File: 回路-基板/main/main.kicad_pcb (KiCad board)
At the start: 2 copper layers, 70 x 70 mm, 31 parts, among them J2 Conn_01x06_Pin, Q1 PNP, Q2 NPN, Q3 PNP, Q4 NPN, SW1 SW_Push, SW2 SW_Push, SW3 SW_Push, SW4 SW_Push, SW5 SW_Push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

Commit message: 回路やり直したよ
山本さんからのアドバイス部分を修正
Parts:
- C1, C2, C3: moved to F.Cu
- moved C3 75.6 mm to (85.5, 101.0), turned to 90 degrees
- moved C2 72.2 mm to (83.0, 101.0), turned to 90 degrees
- moved C1 68.9 mm to (80.5, 101.0), turned to 90 degrees
- moved C4 31.1 mm to (109.2, 139.0)
- moved R3 31.1 mm to (103.3, 146.0)
- moved R4 31.1 mm to (115.2, 139.0)
- moved R5 31.1 mm to (115.2, 141.9)
- moved R7 31.1 mm to (92.9, 141.0)
- moved R8 31.1 mm to (92.9, 143.9)
- moved C5 31.1 mm to (109.2, 143.7)
- moved R6 31.1 mm to (115.2, 144.9)
- moved R9 31.1 mm to (92.9, 146.9)
- moved R1 31.1 mm to (97.1, 145.0)
- moved R2 31.1 mm to (97.1, 147.9)
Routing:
- net VCC: track 37.5 -> 44.9 mm, vias 1 -> 2

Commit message: 回路関連
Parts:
- added C10: 0.1uF, Capacitor_SMD:C_0805_2012Metric, B.Cu at (59.7, 111.4)
- added C6: 0.1uF, Capacitor_SMD:C_0805_2012Metric, B.Cu at (66.2, 111.4)
- added C7: 0.1uF, Capacitor_SMD:C_0805_2012Metric, B.Cu at (72.7, 111.4)
- added C8: 0.1uF, Capacitor_SMD:C_0805_2012Metric, B.Cu at (66.2, 115.9)
- added C9: 0.1uF, Capacitor_SMD:C_0805_2012Metric, B.Cu at (66.2, 107.4)
- added FB: 120Ω, Inductor_SMD:L_0603_1608Metric, B.Cu at (92.2, 114.7)
- added N-R: Jumper_2_Small_Bridged, Jumper:SolderJumper-2_P1.3mm_Bridged_Pad1.0x1.5mm, B.Cu at (97.4, 80.4)
- added N-R: Jumper_2_Small_Bridged, Jumper:SolderJumper-2_P1.3mm_Bridged_Pad1.0x1.5mm, B.Cu at (97.4, 82.9)
- added R: Jumper_2_Small_Open, Jumper:SolderJumper-2_P1.3mm_Open_Pad1.0x1.5mm, B.Cu at (113.2, 82.4)
- added R: Jumper_2_Small_Open, Jumper:SolderJumper-2_P1.3mm_Open_Pad1.0x1.5mm, B.Cu at (113.2, 84.9)
- added R10: 10K, Resistor_SMD:R_0805_2012Metric, B.Cu at (67.5, 77.4)
- added R11: 10K, Resistor_SMD:R_0805_2012Metric, B.Cu at (70.0, 77.4)
- added R12: 100, Resistor_SMD:R_0805_2012Metric, B.Cu at (109.4, 82.4)
- added R13: 100, Resistor_SMD:R_0805_2012Metric, B.Cu at (109.4, 84.9)
- C4, C5: moved to F.Cu
- moved R9 84.1 mm to (91.7, 62.9), turned to -135 degrees
- moved R5 83.5 mm to (89.0, 62.6), turned to 45 degrees
- moved R7 76.6 mm to (93.2, 64.4), turned to -135 degrees
- moved R4 63.8 mm to (57.7, 111.4), turned to 90 degrees
- moved C5 60.3 mm to (73.6, 95.0), turned to 90 degrees
- moved C4 58.2 mm to (71.2, 94.9), turned to 90 degrees
- moved R6 52.6 mm to (74.7, 111.4), turned to 90 degrees
- moved R8 46.9 mm to (66.2, 105.4), turned to 0 degrees
- moved R3 46.5 mm to (66.2, 117.9), turned to 0 degrees
- moved R2 40.4 mm to (66.2, 121.9)
- moved R1 39.8 mm to (66.2, 119.9), turned to 0 degrees
- moved BT1 17.9 mm to (66.2, 94.9)
- moved BT2 17.9 mm to (100.2, 94.9)
- moved C1 17.9 mm to (63.7, 94.9)
- moved C2 17.9 mm to (66.2, 94.9)
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- renumbered Q2 to NPN, Q4 to NPN, Q3 to PNP, Q1 to PNP
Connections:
- J2 pad 4: USB-TX=main -> Net-(J2-Pin_4)
- J2 pad 5: USB-RX=main -> Net-(J2-Pin_5)
- U4 pad 1: +3.3V -> GPS-TX=main
- U4 pad 2: GPS-TX=main -> GND
- U4 pad 4: GND -> unconnected-(U4-BATT-Pad4)
- U4 pad 5: (no net) -> Net-(U4-VCC)
- U4 pad 6: (no net) -> unconnected-(U4-NC-Pad6)
- U4 pad 7: (no net) -> unconnected-(U4-NC-Pad7)
- U4 pad 8: (no net) -> unconnected-(U4-NC-Pad8)
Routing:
- net BTN-CENTER: track 0.00 -> 97.6 mm, vias 0 -> 2
- net BTN-UP: track 0.00 -> 91.3 mm, vias 0 -> 2
- net BTN-LEFT: track 0.00 -> 81.8 mm, vias 0 -> 2
- net BTN-DOWN: track 0.00 -> 72.4 mm, vias 0 -> 2
- net +3.3V: track 59.0 -> 131.1 mm, vias 0 -> 3
- net BTN-RIGHT: track 0.00 -> 68.7 mm, vias 0 -> 2
- net RX=main: track 3.12 -> 47.1 mm, vias 2 -> 3
- net Net-(C10-Pad1): track 0.00 -> 42.7 mm
- net TX=main: track 7.71 -> 38.0 mm, vias 1 -> 0
- net RTS=main: track 0.00 -> 22.7 mm, vias 0 -> 2
- net Net-(J2-Pin_5): track 0.00 -> 21.8 mm
- net Net-(J2-Pin_4): track 0.00 -> 19.4 mm
- net USB-TX=main: track 6.32 -> 23.7 mm, vias 0 -> 1
- net CTS=main: track 0.00 -> 15.4 mm, vias 0 -> 1
- net UART-GPS=ON: track 57.5 -> 68.1 mm
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
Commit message: 事後プレゼンスライド追加
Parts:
- removed BT1, BT2: 3V, @2024-cansat:BHSD-2032-SM
- removed C1, C10, C6, C7, C8, C9: 0.1uF, Capacitor_SMD:C_0805_2012Metric
- removed C2, C4, C5: 10uF, Capacitor_SMD:C_0805_2012Metric
- removed C3: 22uF, Capacitor_SMD:C_0805_2012Metric
- removed FB: 120Ω, Inductor_SMD:L_0603_1608Metric
- removed J2: Conn_01x06_Pin, Connector_PinSocket_2.54mm:PinSocket_1x06_P2.54mm_Horizontal
- removed N-R (x2): Jumper_2_Small_Bridged, Jumper:SolderJumper-2_P1.3mm_Bridged_Pad1.0x1.5mm
- removed NPN (x2): NPN, Package_TO_SOT_SMD:SC-59
- removed PNP (x2): PNP, Package_TO_SOT_SMD:SOT-323_SC-70
- removed R (x2): Jumper_2_Small_Open, Jumper:SolderJumper-2_P1.3mm_Open_Pad1.0x1.5mm
- removed R1, R3, R4, R6, R7, R8, R9: 100k, Resistor_SMD:R_0805_2012Metric
- removed R10, R11: 10K, Resistor_SMD:R_0805_2012Metric
- removed R12, R13: 100, Resistor_SMD:R_0805_2012Metric
- removed R2, R5: 10k, Resistor_SMD:R_0805_2012Metric
- removed SW1, SW2, SW3, SW4, SW5: SW_Push, @2024-cansat:TVBP06-B043C
- removed SW6: SW_SPDT, @2024-cansat:SS12D01G4
- removed U1: TWE-L-WX, RF_Module:MonoWireless_TWE-L-WX
- removed U2: ~, Connector_PinSocket_2.54mm:PinSocket_1x04_P2.54mm_Vertical
- removed U3: LM1117MP-3.3, Package_TO_SOT_SMD:SOT-223-3_TabPin2
- removed U4: ~, @2024-cansat:GPS-54D-014
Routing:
- net +3.3V: track 131.1 -> 0.00 mm, vias 3 -> 0
- net BTN-CENTER: track 97.6 -> 0.00 mm, vias 2 -> 0
- net BTN-UP: track 91.3 -> 0.00 mm, vias 2 -> 0
- net BTN-LEFT: track 81.8 -> 0.00 mm, vias 2 -> 0
- net BTN-DOWN: track 72.4 -> 0.00 mm, vias 2 -> 0
- net BTN-RIGHT: track 68.7 -> 0.00 mm, vias 2 -> 0
- net UART-GPS=ON: track 68.1 -> 0.00 mm, vias 1 -> 0
- net VCC: track 47.4 -> 0.00 mm, vias 2 -> 0
- net RX=main: track 47.1 -> 0.00 mm, vias 3 -> 0
- net Net-(C10-Pad1): track 42.7 -> 0.00 mm
- net SCL: track 40.6 -> 0.00 mm
- net TX=main: track 38.0 -> 0.00 mm
- net SDA: track 33.1 -> 0.00 mm
- net USB-TX=main: track 23.7 -> 0.00 mm, vias 1 -> 0
- net UART-USB=ON: track 22.9 -> 0.00 mm
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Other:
- board size 70 x 70 mm -> 60 x 60 mm
- board text added: "・TWE-LITEのアンテナは中心になってはいけない （重ねたときに互い違いにするため） アンテナ筒の外径=8mm →最低4mmずらすことが必要 ・原点中心で対角に穴を作る（最低直径3mm）"

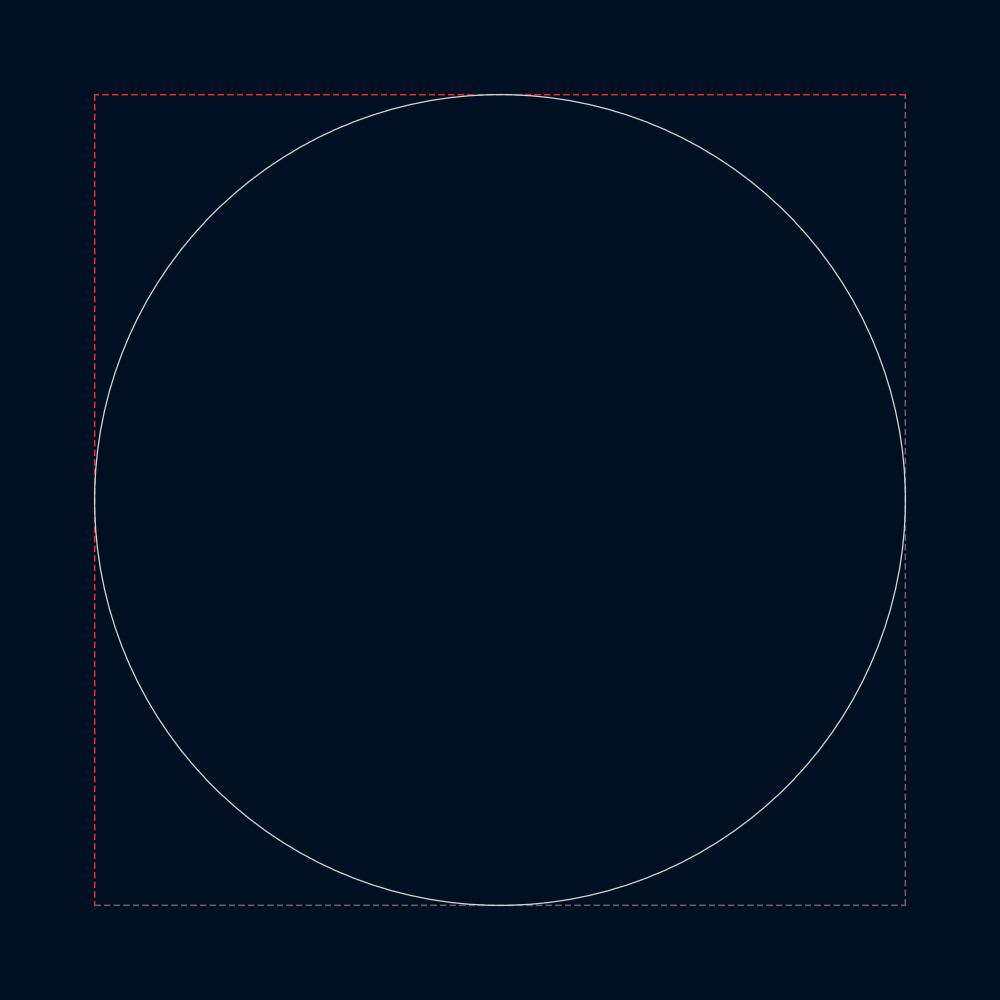
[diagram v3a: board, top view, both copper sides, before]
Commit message: 回路図を修正、PCBを作成し始めた（直径60）
電池の配置場所がわからん...
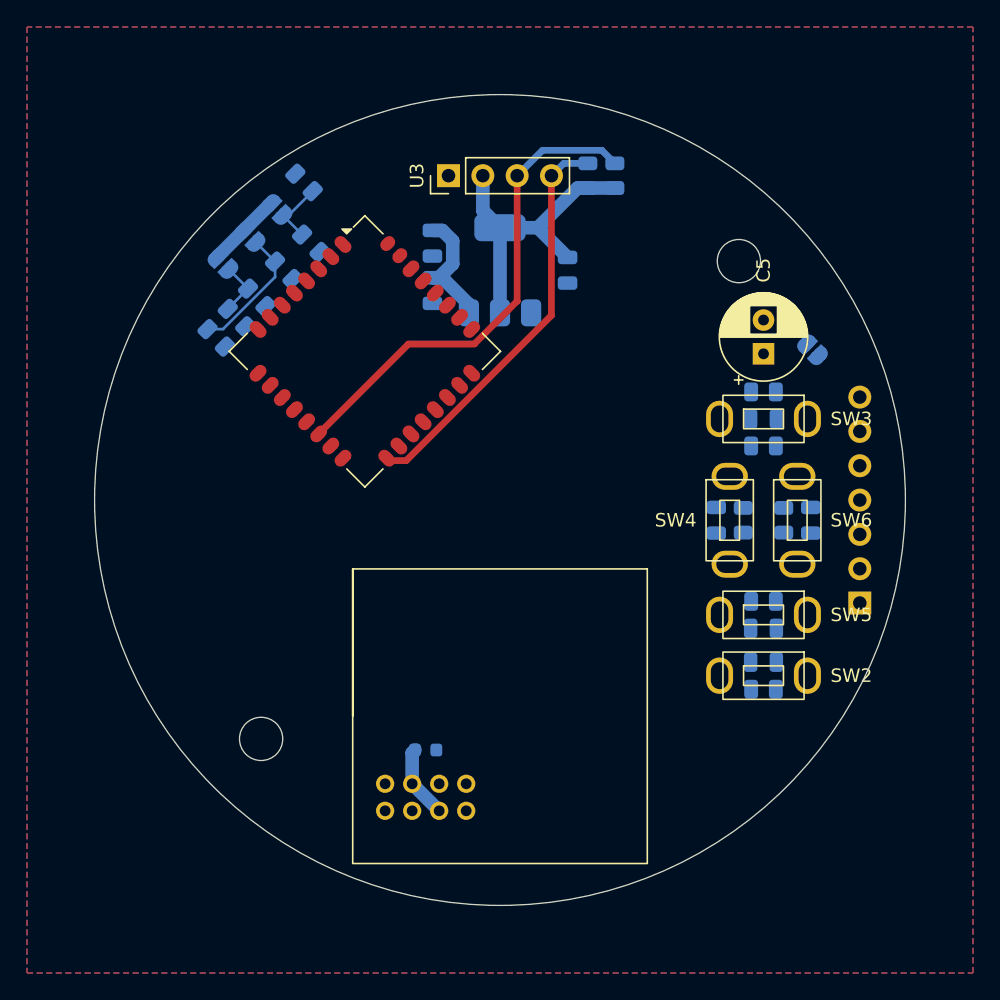
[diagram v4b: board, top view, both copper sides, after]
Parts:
- added C1: 0.1uF, Capacitor_SMD:C_0805_2012Metric, B.Cu at (-5.00, -19.0)
- added C10: 0.1uF, Capacitor_SMD:C_0805_2012Metric, B.Cu at (23.0, 1.50)
- added C3: 10uF, Capacitor_SMD:C_0805_2012Metric, B.Cu at (-5.00, -15.5)
- added C4: 10uF, Capacitor_SMD:C_0805_2012Metric, B.Cu at (5.00, -17.0)
- added C5: 100uF, Capacitor_THT:CP_Radial_D6.3mm_P2.50mm, F.Cu at (19.5, -10.8)
- added C6: 0.1uF, Capacitor_SMD:C_0805_2012Metric, B.Cu at (19.5, 12.0)
- added C7: 0.1uF, Capacitor_SMD:C_0805_2012Metric, B.Cu at (19.5, -6.00)
- added C8: 0.1uF, Capacitor_SMD:C_0805_2012Metric, B.Cu at (16.0, 1.50)
- added C9: 0.1uF, Capacitor_SMD:C_0805_2012Metric, B.Cu at (19.5, 9.50)
- added FB1: FerriteBead_Small, Inductor_SMD:L_0603_1608Metric, B.Cu at (-5.50, 18.5)
- added J1: Conn_01x07_Pin, Connector_PinHeader_2.54mm:PinHeader_1x07_P2.54mm_Horizontal, B.Cu at (26.6, 7.62)
- added JP1: Jumper_2_Small_Open, Jumper:SolderJumper-2_P1.3mm_Open_RoundedPad1.0x1.5mm, B.Cu at (23.1, -11.1)
- added JP2: Jumper_2_Small_Open, Jumper:SolderJumper-2_P1.3mm_Open_RoundedPad1.0x1.5mm, B.Cu at (-16.5, -21.5)
- added JP3: Jumper_2_Small_Open, Jumper:SolderJumper-2_P1.3mm_Open_RoundedPad1.0x1.5mm, B.Cu at (-18.5, -19.5)
- added JP4: Jumper_2_Small_Open, Jumper:SolderJumper-2_P1.3mm_Open_RoundedPad1.0x1.5mm, B.Cu at (-20.5, -17.5)
- added R10: 10K, Resistor_SMD:R_0805_2012Metric, B.Cu at (8.50, -24.0)
- added R11: 10K, Resistor_SMD:R_0805_2012Metric, B.Cu at (6.50, -24.0)
- added R12: 100k, Resistor_SMD:R_0805_2012Metric, B.Cu at (19.5, 14.0)
- added R13: 100k, Resistor_SMD:R_0805_2012Metric, B.Cu at (19.5, -4.00)
- added R14: 100k, Resistor_SMD:R_0805_2012Metric, B.Cu at (18.0, 1.50)
- added R15: 100k, Resistor_SMD:R_0805_2012Metric, B.Cu at (19.5, 7.50)
- added R16: 100k, Resistor_SMD:R_0805_2012Metric, B.Cu at (21.0, 1.50)
- added R17: 10k, Resistor_SMD:R_0805_2012Metric, B.Cu at (19.5, -8.00)
- added R4: 1K, Resistor_SMD:R_0805_2012Metric, B.Cu at (-14.0, -19.0)
- added R5: 10K, Resistor_SMD:R_0805_2012Metric, B.Cu at (-14.5, -23.5)
- added R6: 1K, Resistor_SMD:R_0805_2012Metric, B.Cu at (-16.0, -17.0)
- added R7: 10K, Resistor_SMD:R_0805_2012Metric, B.Cu at (-21.0, -12.0)
- added R8: 1K, Resistor_SMD:R_0805_2012Metric, B.Cu at (-18.0, -15.0)
- added R9: 10K, Resistor_SMD:R_0805_2012Metric, B.Cu at (-19.5, -13.5)
- added REF**: MountingHole_3.2mm_M3, MountingHole:MountingHole_3.2mm_M3, F.Cu at (-17.7, 17.7)
- added REF**: MountingHole_3.2mm_M3, MountingHole:MountingHole_3.2mm_M3, F.Cu at (17.7, -17.7)
- added SW2: SW_Push, @2024-cansat:TVBP06-B043C, F.Cu at (19.5, 13.0)
- added SW3: SW_Push, @2024-cansat:TVBP06-B043C, F.Cu at (19.5, -6.00)
- added SW4: SW_Push, @2024-cansat:TVBP06-B043C, F.Cu at (17.0, 1.50)
- added SW5: SW_Push, @2024-cansat:TVBP06-B043C, F.Cu at (19.5, 8.50)
- added SW6: SW_Push, @2024-cansat:TVBP06-B043C, F.Cu at (22.0, 1.50)
- added U1: TWE-L-WX, RF_Module:MonoWireless_TWE-L-WX, F.Cu at (-10.0, -11.0)
- added U2: LM1117MP-3.3, Package_TO_SOT_SMD:SOT-223-3_TabPin2, B.Cu at (0.00, -17.0)
- added U3: ~, @2024-cansat:Display, F.Cu at (0.00, -24.0)
- added U4: ~, @2024-cansat:GPS-54D-014, F.Cu at (0.00, 16.0)
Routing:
- net 14: track 0.00 -> 36.4 mm
- net 17: track 0.00 -> 30.1 mm
- net +3.3V: track 0.00 -> 29.2 mm
- net Net-(JP3-A): track 0.00 -> 9.72 mm
- net VCC: track 0.00 -> 9.59 mm
- net Net-(U4-BATT): track 0.00 -> 5.42 mm
- net Net-(JP2-A): track 0.00 -> 4.91 mm
- net Net-(JP4-A): track 0.00 -> 4.09 mm
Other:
- board text removed: "・TWE-LITEのアンテナは中心になってはいけない （重ねたときに互い違いにするため） アンテナ筒の外径=8mm →最低4mmずらすことが必要 ・原点中心で対角に穴を作る（最低直径3mm）"

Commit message: PCBデザインを更新
単4電池3本分のサイズをとってみた、きつい
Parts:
- C1, C3, C4, JP2, JP3, JP4, R4, R5, R6, R7, R8, R9, U2: moved to F.Cu
- moved R4 35.0 mm to (-43.2, 0.34), turned to 0 degrees
- moved R6 33.9 mm to (-43.2, 3.17), turned to 0 degrees
- moved R8 32.8 mm to (-43.2, 6.00), turned to 0 degrees
- moved R5 32.8 mm to (-39.6, -2.49), turned to 180 degrees
- moved R9 32.1 mm to (-43.2, 8.12), turned to 0 degrees
- moved JP2 31.8 mm to (-39.6, 0.34), turned to 0 degrees
- moved R7 31.4 mm to (-43.2, 10.2), turned to 0 degrees
- moved JP3 31.0 mm to (-39.6, 3.17), turned to 0 degrees
- moved JP4 30.3 mm to (-39.6, 6.00), turned to 0 degrees
- moved C3 8.06 mm to (-6.00, -23.5), turned to 180 degrees
- moved C4 6.58 mm to (6.00, -23.5), turned to 0 degrees
- moved C1 6.36 mm to (-9.50, -23.5), turned to 0 degrees
- moved U2 3.50 mm to (0.00, -20.5), turned to -90 degrees
- moved U3 3.50 mm to (0.00, -27.5)
- moved FB1 2.50 mm to (-5.50, 21.0)
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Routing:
- net +3.3V: track 29.2 -> 0.00 mm
- net 14: track 36.4 -> 9.22 mm
- net 17: track 30.1 -> 3.35 mm
- net Net-(JP3-A): track 9.72 -> 0.00 mm
- net VCC: track 9.59 -> 0.00 mm
- net Net-(JP2-A): track 4.91 -> 0.00 mm
- net Net-(JP4-A): track 4.09 -> 0.00 mm

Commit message: 回路図/PCB両方一応完成した
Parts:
- removed C10: 0.1uF, Capacitor_SMD:C_0805_2012Metric
- removed JP1, JP2, JP3, JP4: Jumper_2_Small_Open, Jumper:SolderJumper-2_P1.3mm_Open_RoundedPad1.0x1.5mm
- removed R15, R16: 100k, Resistor_SMD:R_0805_2012Metric
- removed R17: 10k, Resistor_SMD:R_0805_2012Metric
- removed SW6: SW_Push, @2024-cansat:TVBP06-B043C
- added BT1: 1.5V, @2024-cansat:AAA-holder, B.Cu at (12.0, -22.4)
- added BT2: 1.5V, @2024-cansat:AAA-holder, B.Cu at (0.00, 22.4)
- added BT3: 1.5V, @2024-cansat:AAA-holder, B.Cu at (-12.0, -22.4)
- added C2: 10uF, Capacitor_SMD:C_0805_2012Metric, F.Cu at (-16.0, -13.0)
- added J2: Conn_01x08_Pin, @2024-cansat:Pin-Extender, F.Cu at (16.4, -20.1)
- added J3: Conn_01x08_Pin, @2024-cansat:Pin-Extender, F.Cu at (2.44, -14.9)
- added J4: Conn_01x08_Pin, @2024-cansat:Pin-Extender, F.Cu at (7.55, -0.94)
- added J5: Conn_01x08_Pin, @2024-cansat:Pin-Extender, F.Cu at (21.6, -6.05)
- added M1: Jumper_2_Small_Open, Jumper:SolderJumper-2_P1.3mm_Open_RoundedPad1.0x1.5mm, B.Cu at (-2.50, -16.0)
- added M2: Jumper_2_Small_Open, Jumper:SolderJumper-2_P1.3mm_Open_RoundedPad1.0x1.5mm, B.Cu at (-2.50, -11.5)
- added M3: Jumper_2_Small_Open, Jumper:SolderJumper-2_P1.3mm_Open_RoundedPad1.0x1.5mm, B.Cu at (-2.50, -7.00)
- added R1: 1K, Resistor_SMD:R_0805_2012Metric, F.Cu at (-2.50, -17.0)
- added R2: 10K, Resistor_SMD:R_0805_2012Metric, F.Cu at (-2.50, -15.0)
- added R3: 1K, Resistor_SMD:R_0805_2012Metric, F.Cu at (-2.50, -12.5)
- added SW1: SW_Push, @2024-cansat:TVBP06-B043C, F.Cu at (12.0, 11.0)
- added VBUS/+3.3V: Jumper_2_Small_Open, Jumper:SolderJumper-2_P1.3mm_Open_RoundedPad1.0x1.5mm, B.Cu at (22.9, 0.50)
- C4: value 10uF -> 100uF; footprint Capacitor_SMD:C_0805_2012Metric -> Capacitor_THT:CP_Radial_D6.3mm_P2.50mm
- C5: value 100uF -> 0.1uF; footprint Capacitor_THT:CP_Radial_D6.3mm_P2.50mm -> Capacitor_SMD:C_0805_2012Metric
- C6, C7, C8, C9, FB1, R12, R13: moved to F.Cu
- J1: footprint Connector_PinHeader_2.54mm:PinHeader_1x07_P2.54mm_Horizontal -> Connector_PinSocket_2.54mm:PinSocket_1x07_P2.54mm_Vertical; moved to F.Cu
- R10, R11: value 10K -> 100k; moved to F.Cu
- R14: value 100k -> 10k; moved to F.Cu
- R4, R6, R8: value 1K -> 10K
- R5: value 10K -> 1K
- R9: value 10K -> 100k
- moved R8 59.3 mm to (7.00, -25.5), turned to 90 degrees
- moved R9 57.2 mm to (14.0, 8.00), turned to 180 degrees
- moved R7 50.9 mm to (-7.00, -25.5), turned to 90 degrees
- moved R4 42.1 mm to (-2.50, -10.5)
- moved R6 41.7 mm to (-2.50, -6.00)
- moved REF** 37.6 mm to (19.9, 18.2), turned to 2.5 degrees
- moved REF** 37.6 mm to (-19.9, -18.2), turned to 2.5 degrees
- moved R5 37.6 mm to (-2.50, -8.00)
- moved R11 33.9 mm to (1.00, 8.50), turned to -90 degrees
- moved C4 29.8 mm to (-20.5, -9.85), turned to 180 degrees
- moved FB1 28.2 mm to (-19.5, -3.50)
- moved R10 26.6 mm to (14.0, 1.00), turned to 180 degrees
- moved C7 26.2 mm to (1.00, 12.5), turned to 90 degrees
- moved SW3 23.0 mm to (4.00, 11.0), turned to -90 degrees
- moved U1 22.0 mm to (12.0, -10.5), turned to -90 degrees
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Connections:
- C3 pad 1: VCC -> +3.3V
- C5 pad 1: +3.3V -> Net-(C5-Pad1)
- C5 pad 2: GND -> 23
- C6 pad 1: Net-(C10-Pad1) -> Net-(C5-Pad1)
- C6 pad 2: BTN-CENTER -> 25
- C7 pad 1: Net-(C10-Pad1) -> Net-(C5-Pad1)
- C7 pad 2: BTN-UP -> 22
- C8 pad 1: Net-(C10-Pad1) -> Net-(C5-Pad1)
- C8 pad 2: BTN-LEFT -> 19
- C9 pad 1: Net-(C10-Pad1) -> Net-(C5-Pad1)
- C9 pad 2: BTN-DOWN -> 24
- J1 pad 6: +3.3V -> Net-(J1-Pin_6)
- J1 pad 7: Net-(J1-Pin_7) -> unconnected-(J1-Pin_7-Pad7)
- R10 pad 1: +3.3V -> GND
- R10 pad 2: 14 -> 25
- R11 pad 1: +3.3V -> GND
- R11 pad 2: 17 -> 22
- R12 pad 2: BTN-CENTER -> 19
- R13 pad 2: BTN-UP -> 24
- R14 pad 1: GND -> +3.3V
- R14 pad 2: BTN-LEFT -> Net-(C5-Pad1)
- R4 pad 1: 12 -> GND
- R4 pad 2: Net-(JP2-A) -> Net-(JP3-A)
- R5 pad 1: GND -> 27
- R5 pad 2: Net-(JP2-A) -> Net-(JP4-A)
- R6 pad 1: 26 -> GND
- R6 pad 2: Net-(JP3-A) -> Net-(JP4-A)
- R7 pad 1: GND -> +3.3V
- R7 pad 2: Net-(JP3-A) -> 14
- R8 pad 1: 27 -> +3.3V
- R8 pad 2: Net-(JP4-A) -> 17
- R9 pad 2: Net-(JP4-A) -> 23
- SW2 pad 1: BTN-CENTER -> 25
- SW2 pad 2: Net-(C10-Pad1) -> Net-(C5-Pad1)
- SW3 pad 1: BTN-UP -> 22
- SW3 pad 2: Net-(C10-Pad1) -> Net-(C5-Pad1)
- SW4 pad 1: BTN-LEFT -> 19
- SW4 pad 2: Net-(C10-Pad1) -> Net-(C5-Pad1)
- SW5 pad 1: BTN-DOWN -> 24
- SW5 pad 2: Net-(C10-Pad1) -> Net-(C5-Pad1)
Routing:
- net +3.3V: track 0.00 -> 155.7 mm, vias 0 -> 3
- net 8: track 0.00 -> 80.2 mm, vias 0 -> 3
- net 9: track 0.25 -> 80.1 mm, vias 0 -> 1
- net Net-(C5-Pad1): track 0.00 -> 58.4 mm
- net 19: track 0.00 -> 40.7 mm
- net 26: track 0.00 -> 34.8 mm, vias 0 -> 1
- net 27: track 0.00 -> 31.5 mm, vias 0 -> 1
- net 17: track 3.35 -> 31.8 mm
- net 2: track 0.00 -> 28.2 mm
- net 14: track 9.22 -> 33.4 mm
- net 22: track 0.00 -> 23.4 mm
- net 21: track 0.00 -> 23.0 mm, vias 0 -> 2
- net 23: track 0.00 -> 22.0 mm
- net 25: track 0.00 -> 21.5 mm
- net 24: track 0.00 -> 19.0 mm
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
